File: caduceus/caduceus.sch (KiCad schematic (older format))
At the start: 14 parts

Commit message: Forgot to press save
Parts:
- added C?: 1uF, symbol Device:C
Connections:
- net GND: now also C?.2
- net at U?.4 (PA03): now also C?.1
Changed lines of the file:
@@
 Wire Wire Line
 	5150 3650 5250 3650
+Wire Wire Line
+	3850 2950 3950 2950
+$Comp
+L Device:C C?
+U 1 1 5F6D5ECB
+P 3700 2950
+F 0 "C?" V 3550 2950 50  0000 C CNN
+F 1 "1uF" V 3750 3100 50  0000 C CNN
+F 2 "" H 3738 2800 50  0001 C CNN
+F 3 "~" H 3700 2950 50  0001 C CNN
+	1    3700 2950
+	0    1    1    0
+$EndComp
+Wire Wire Line
+	3550 2950 3450 2950
+$Comp
+L power:GND #PWR?
+U 1 1 5F6D874C
+P 3450 2950
+F 0 "#PWR?" H 3450 2700 50  0001 C CNN
+F 1 "GND" V 3455 2822 50  0000 R CNN
+F 2 "" H 3450 2950 50  0001 C CNN
+F 3 "" H 3450 2950 50  0001 C CNN
+	1    3450 2950
+	0    1    1    0
+$EndComp
 $EndSCHEMATC

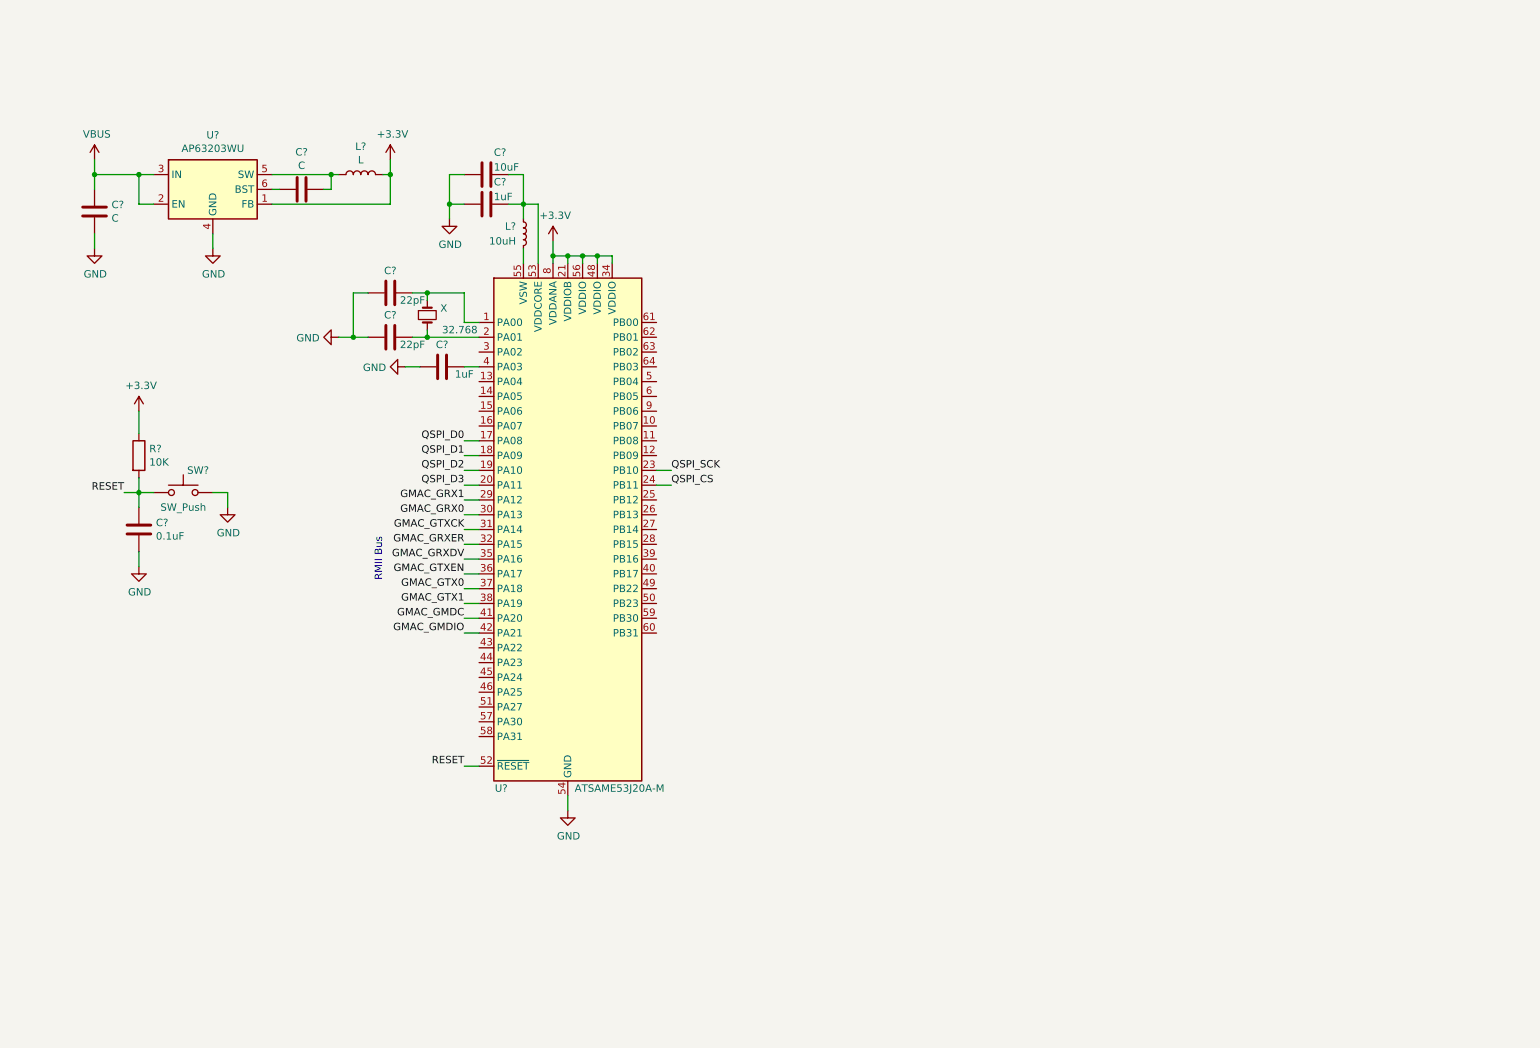
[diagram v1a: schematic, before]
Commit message: Added transceiver and T1 input
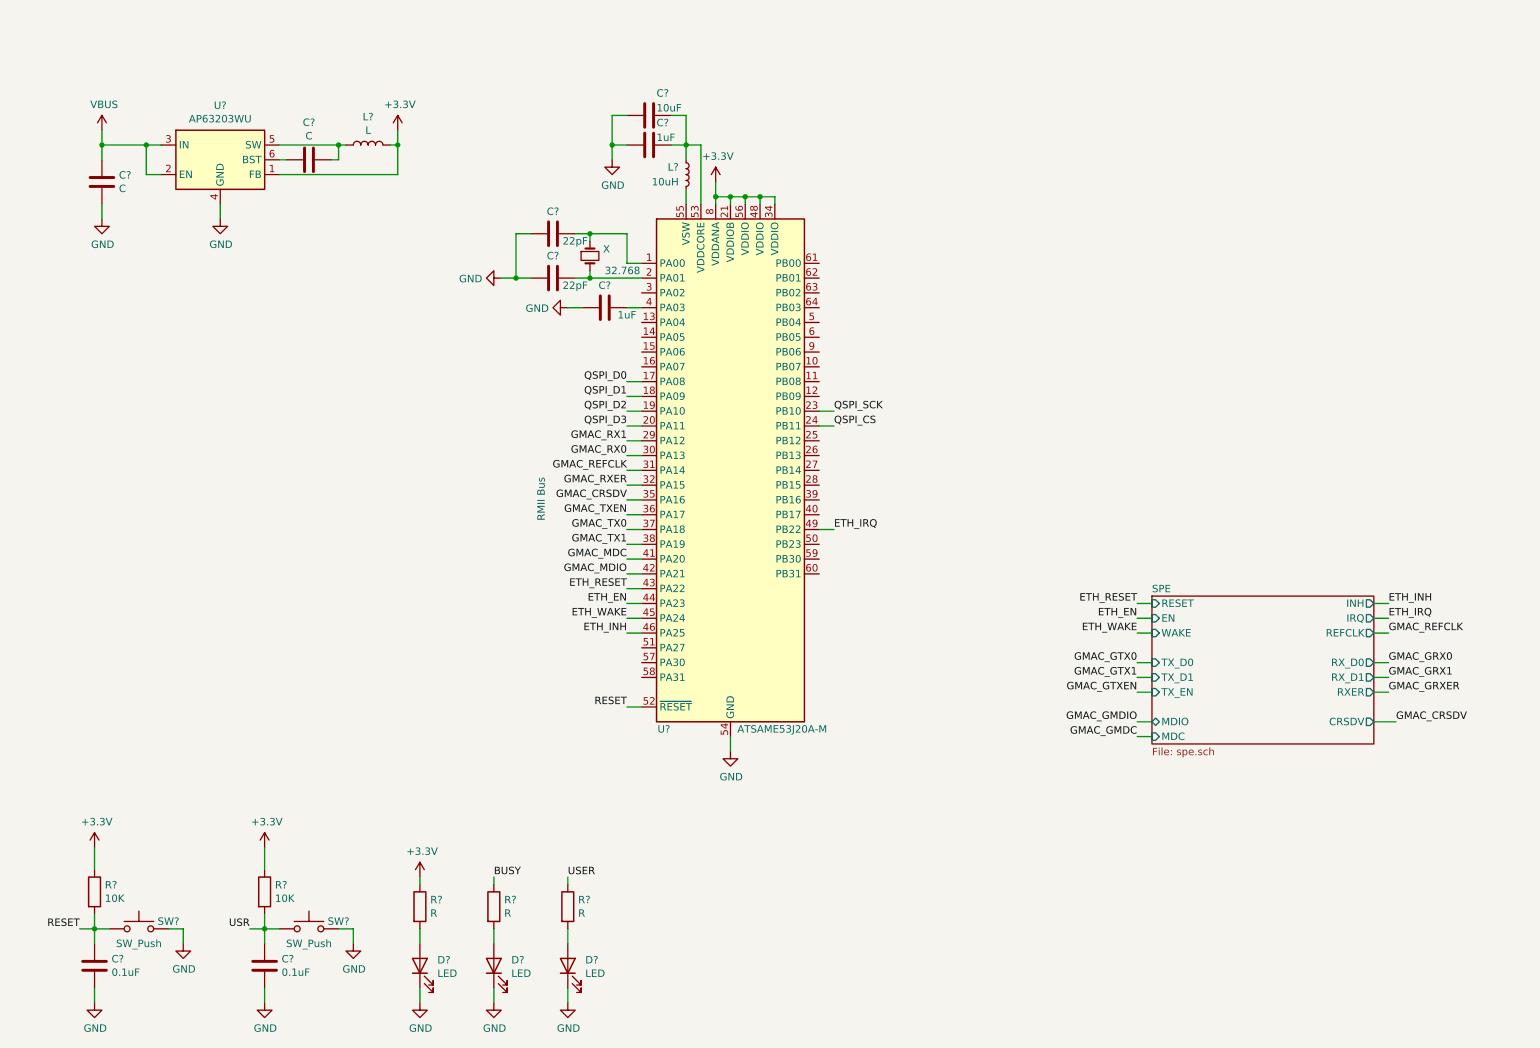
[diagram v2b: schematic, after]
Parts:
- added C?: 0.1uF, symbol Device:C
- added D? (x3): LED, symbol Device:LED
- added R?: 10K, symbol Device:R
- added R? (x3): R, symbol Device:R
- added SW?: SW_Push, symbol Switch:SW_Push
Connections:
- net +3V3: now also R?.1, R?.1
- net GMAC_GMDC: no longer U?.41 (PA20)
- net GMAC_GMDIO: no longer U?.42 (PA21)
- net GMAC_GRX0: no longer U?.30 (PA13)
- net GMAC_GRX1: no longer U?.29 (PA12)
- net GMAC_GRXER: no longer U?.32 (PA15)
- net GMAC_GTX0: no longer U?.37 (PA18)
- net GMAC_GTX1: no longer U?.38 (PA19)
- net GMAC_GTXEN: no longer U?.36 (PA17)
- net GND: now also C?.2, D?.1 (K), D?.1 (K), D?.1 (K), SW?.2
- net ETH_RESET: now reaches U?.43 (PA22)
- net ETH_EN: now reaches U?.44 (PA23)
- net ETH_WAKE: now reaches U?.45 (PA24)
- net ETH_INH: now reaches U?.46 (PA25)
- net ETH_IRQ: now reaches U?.49 (PB22)
- net GMAC_GRXDV renamed GMAC_CRSDV
- net GMAC_GTXCK renamed GMAC_REFCLK
- new net: D?.2 (A), R?.2 (x3)
- new net BUSY: R?.1
- new net GMAC_MDC: U?.41 (PA20)
- new net GMAC_MDIO: U?.42 (PA21)
- new net GMAC_RX0: U?.30 (PA13)
- new net GMAC_RX1: U?.29 (PA12)
- new net GMAC_RXER: U?.32 (PA15)
- new net GMAC_TX0: U?.37 (PA18)
- new net GMAC_TX1: U?.38 (PA19)
- new net GMAC_TXEN: U?.36 (PA17)
- new net USER: R?.1
- new net USR: C?.1, R?.2, SW?.1
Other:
- moved on the sheet: C?, L?, R?, SW?, U?, X

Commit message: Added USB, resolved regulation, added headers, updated apperance of ethernet interface, added QSPI flash. Meant to add to devel branch but happened on master. Schematic basically done, requires review
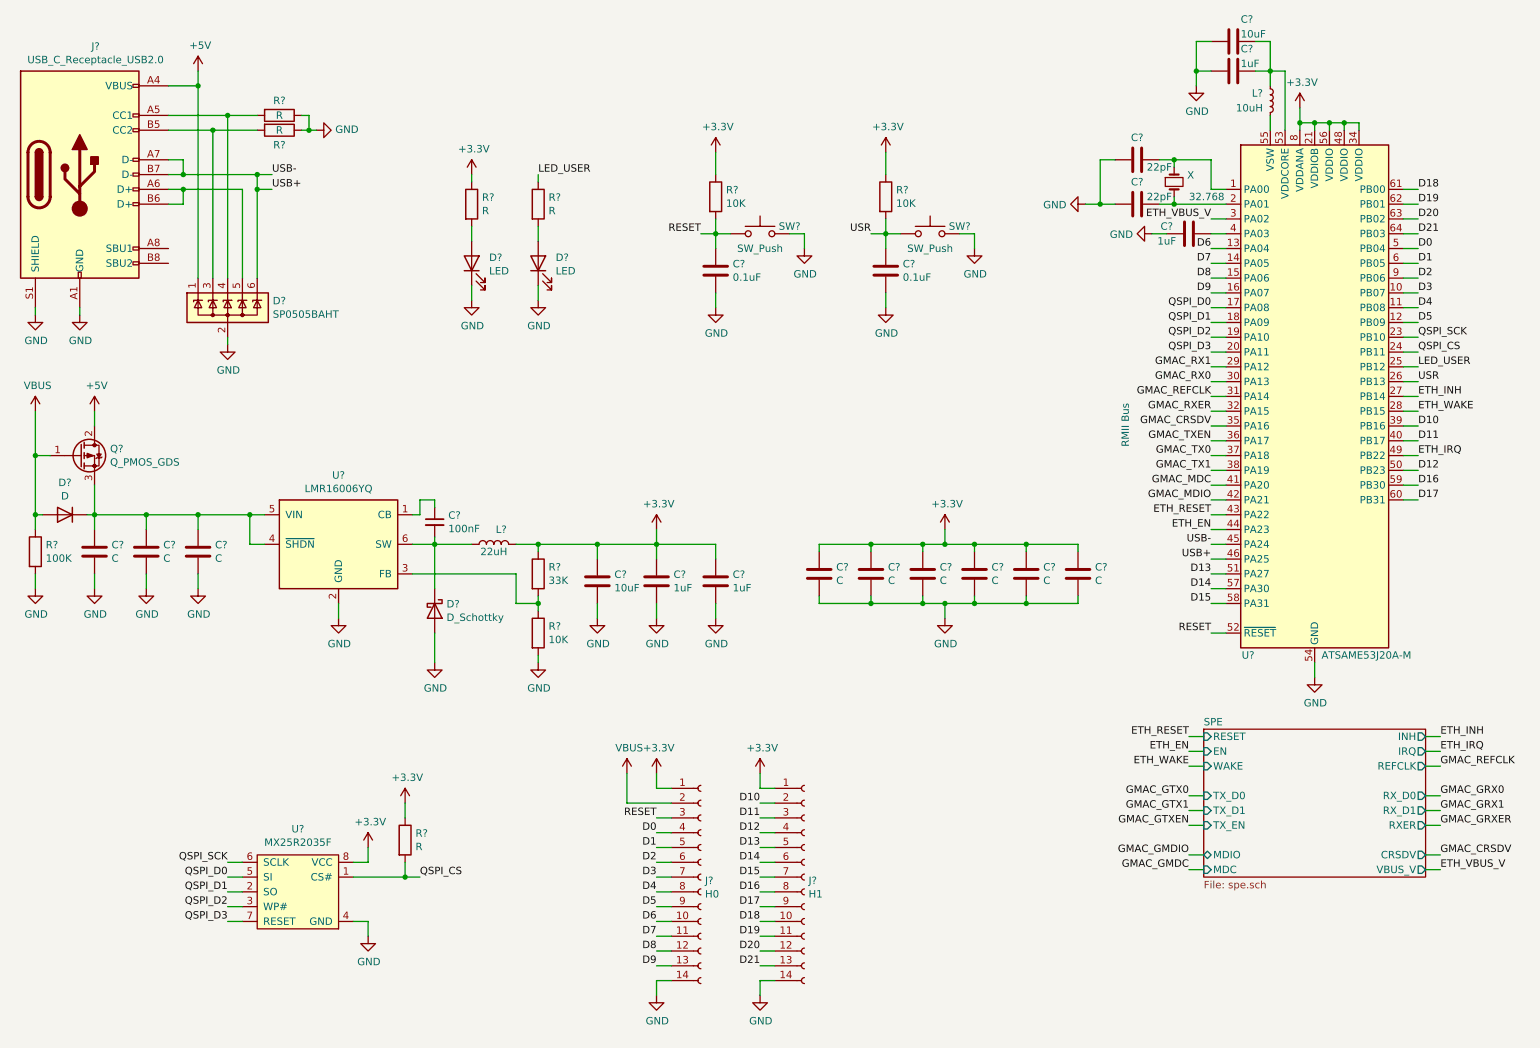
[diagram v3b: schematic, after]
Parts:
- removed C? (x2): C, symbol Device:C
- removed D?: LED, symbol Device:LED
- removed L?: L, symbol Device:L
- removed R?: R, symbol Device:R
- removed U?: AP63203WU, Package_TO_SOT_SMD:TSOT-23-6, symbol Regulator_Switching:AP63203WU
- added C? (x9): C, symbol Device:C
- added C?: 100nF, symbol Device:C_Small
- added C?: 10uF, symbol Device:C
- added C? (x2): 1uF, symbol Device:C
- added D?: SP0505BAHT, Package_TO_SOT_SMD:SOT-23-6, symbol Power_Protection:SP0505BAHT
- added D?: D, symbol Device:D
- added D?: D_Schottky, symbol Device:D_Schottky
- added J?: USB_C_Receptacle_USB2.0, symbol Connector:USB_C_Receptacle_USB2.0
- added J?: H1, symbol Connector:Conn_01x14_Female
- added J?: H0, symbol Connector:Conn_01x14_Female
- added L?: 22uH, symbol Device:L
- added Q?: Q_PMOS_GDS, symbol Device:Q_PMOS_GDS
- added R? (x3): R, symbol Device:R
- added R?: 100K, symbol Device:R
- added R?: 33K, symbol Device:R
- added R?: 10K, symbol Device:R
- added U?: LMR16006YQ, Package_TO_SOT_SMD:SOT-23-6, symbol Regulator_Switching:LMR16006YQ
- added U?: MX25R2035F, symbol caduceus:MX25R2035F
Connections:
- net USER is gone; now on net LED_USER: R?.1
- net +3V3: now also C?.1, C?.1, C?.1, C?.1, C?.1, C?.1, C?.1, C?.1, C?.1, J?.1 (Pin_1), J?.1 (Pin_1), L?.2, R?.1, R?.1, U?.8 (VCC)
- net ETH_INH: now also U?.27 (PB14); no longer U?.46 (PA25)
- net ETH_WAKE: now also U?.28 (PB15); no longer U?.45 (PA24)
- net GND: now also C?.2, C?.2, C?.2, C?.2, C?.2, C?.2, C?.2, C?.2, C?.2, C?.2, C?.2, C?.2, D?.2 (A), D?.2 (A), J?.14 (Pin_14), J?.14 (Pin_14), J?.A1 (GND), J?.A12 (GND), J?.B1 (GND), J?.B12 (GND), J?.S1 (SHIELD), R?.1, R?.1, R?.2, R?.2, U?.2 (GND), U?.4 (GND)
- net QSPI_CS: now also R?.2, U?.1 (CS#)
- net QSPI_D0: now also U?.5 (SI)
- net QSPI_D1: now also U?.2 (SO)
- net QSPI_D2: now also U?.3 (WP#)
- net QSPI_D3: now also U?.7 (RESET)
- net QSPI_SCK: now also U?.6 (SCLK)
- net RESET: now also J?.3 (Pin_3)
- net USR: now also U?.26 (PB13)
- net VBUS: now also D?.2 (A), J?.2 (Pin_2), Q?.1 (G), R?.1
- net D3: now reaches U?.10 (PB07)
- net D3: now also J?.7 (Pin_7)
- net D4: now reaches U?.11 (PB08)
- net D4: now also J?.8 (Pin_8)
- net D5: now reaches U?.12 (PB09)
- net D5: now also J?.9 (Pin_9)
- net D6: now reaches U?.13 (PA04)
- net D6: now also J?.10 (Pin_10)
- net D7: now reaches U?.14 (PA05)
- net D7: now also J?.11 (Pin_11)
- net D8: now reaches U?.15 (PA06)
- net D8: now also J?.12 (Pin_12)
- net D9: now reaches U?.16 (PA07)
- net D9: now also J?.13 (Pin_13)
- net LED_USER: now reaches U?.25 (PB12)
- net ETH_VBUS_V: now reaches U?.3 (PA02)
- net D10: now reaches U?.39 (PB16)
- net D10: now also J?.2 (Pin_2)
- net D11: now reaches U?.40 (PB17)
- net D11: now also J?.3 (Pin_3)
- net D0: now reaches U?.5 (PB04)
- net D0: now also J?.4 (Pin_4)
- net D12: now reaches U?.50 (PB23)
- net D12: now also J?.4 (Pin_4)
- net D13: now reaches U?.51 (PA27)
- net D13: now also J?.5 (Pin_5)
- net D14: now reaches U?.57 (PA30)
- net D14: now also J?.6 (Pin_6)
- net D15: now reaches U?.58 (PA31)
- net D15: now also J?.7 (Pin_7)
- net D16: now reaches U?.59 (PB30)
- net D16: now also J?.8 (Pin_8)
- net D1: now reaches U?.6 (PB05)
- net D1: now also J?.5 (Pin_5)
- net D17: now reaches U?.60 (PB31)
- net D17: now also J?.9 (Pin_9)
- net D18: now reaches U?.61 (PB00)
- net D18: now also J?.10 (Pin_10)
- net D19: now reaches U?.62 (PB01)
- net D19: now also J?.11 (Pin_11)
- net D20: now reaches U?.63 (PB02)
- net D20: now also J?.12 (Pin_12)
- net D21: now reaches U?.64 (PB03)
- net D21: now also J?.13 (Pin_13)
- net D2: now reaches U?.9 (PB06)
- net D2: now also J?.6 (Pin_6)
- new net: D?.4 (K), J?.A5 (CC1), R?.2
- new net: D?.5 (K), J?.A6 (D+), J?.B6 (D+)
- new net: D?.3 (K), J?.B5 (CC2), R?.2
- new net: C?.1, C?.1, C?.1, D?.1 (K), Q?.3 (S), U?.4 (~SHDN), U?.5 (VIN)
- new net: C?.2, D?.1 (K), L?.1, U?.6 (SW)
- new net: C?.1, U?.1 (CB)
- new net: R?.1, R?.2, U?.3 (FB)
- new net +5V: D?.1 (K), J?.A4 (VBUS), J?.A9 (VBUS), J?.B4 (VBUS), J?.B9 (VBUS), Q?.2 (D)
- new net USB+: D?.6 (K), J?.A7 (D-), J?.B7 (D-), U?.45 (PA24), U?.46 (PA25)
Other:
- moved on the sheet: C?, D?, L?, R?, SW?, U?, X
